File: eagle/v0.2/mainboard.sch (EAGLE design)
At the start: 40 parts, among them IC1 74HCT151D, IC2 74HCT151D, IC3 74HCT151D, IC4 74HCT151D, IC5 74HCT151D, IC6 74HCT151D, IC7 74HC590D, IC8 74HC02D, J1 629722000214, J2 629722000214, J3 629722000214, J4 629722000214, J5 629722000214, J7 L77HDE15SD1CH4RHNVGA

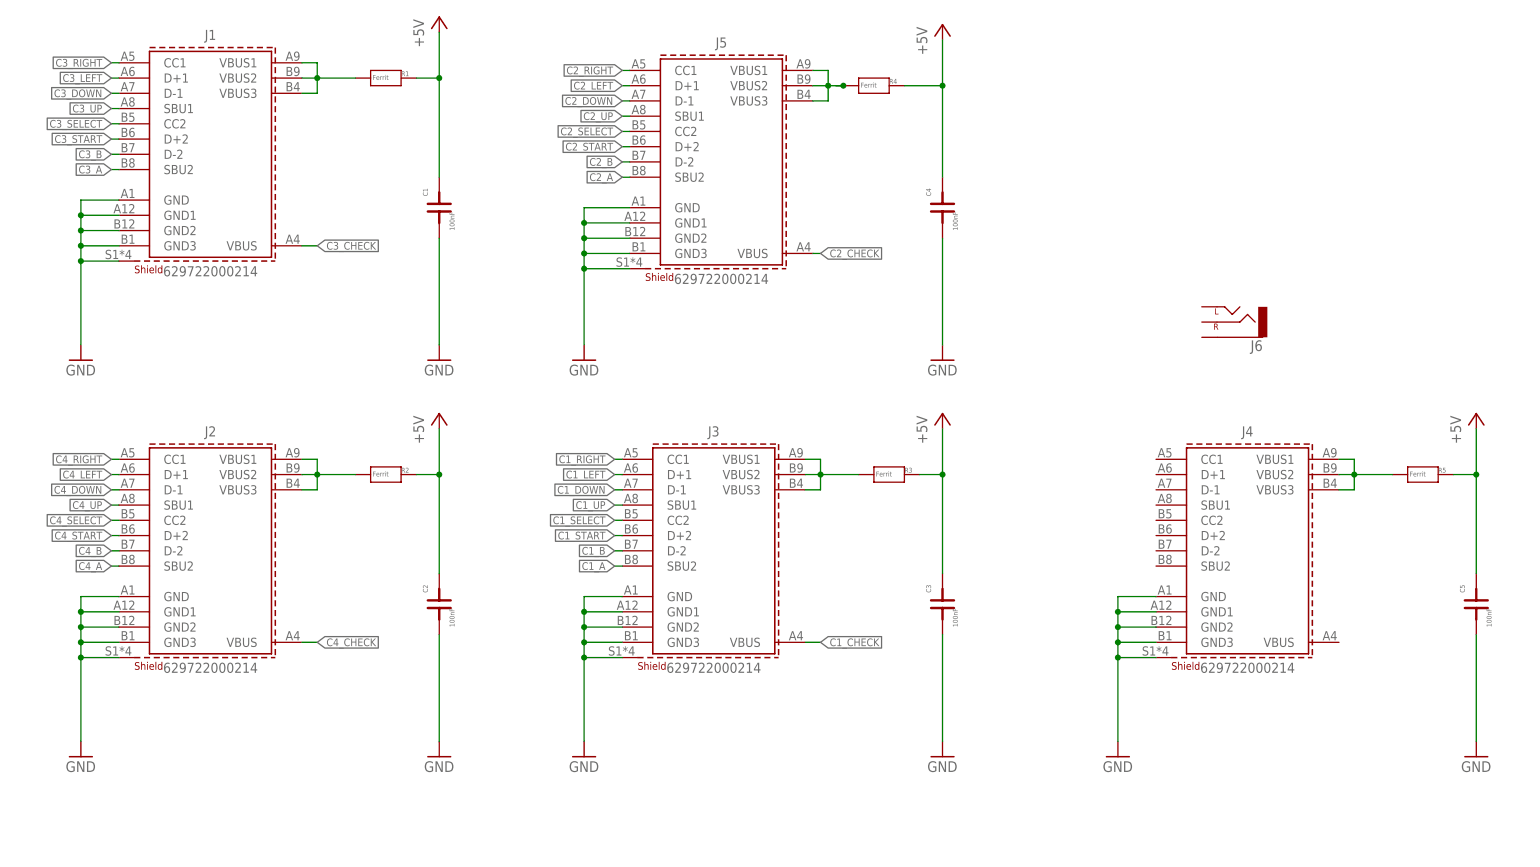
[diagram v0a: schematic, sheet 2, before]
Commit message: updated USB-C receptacles and würth library
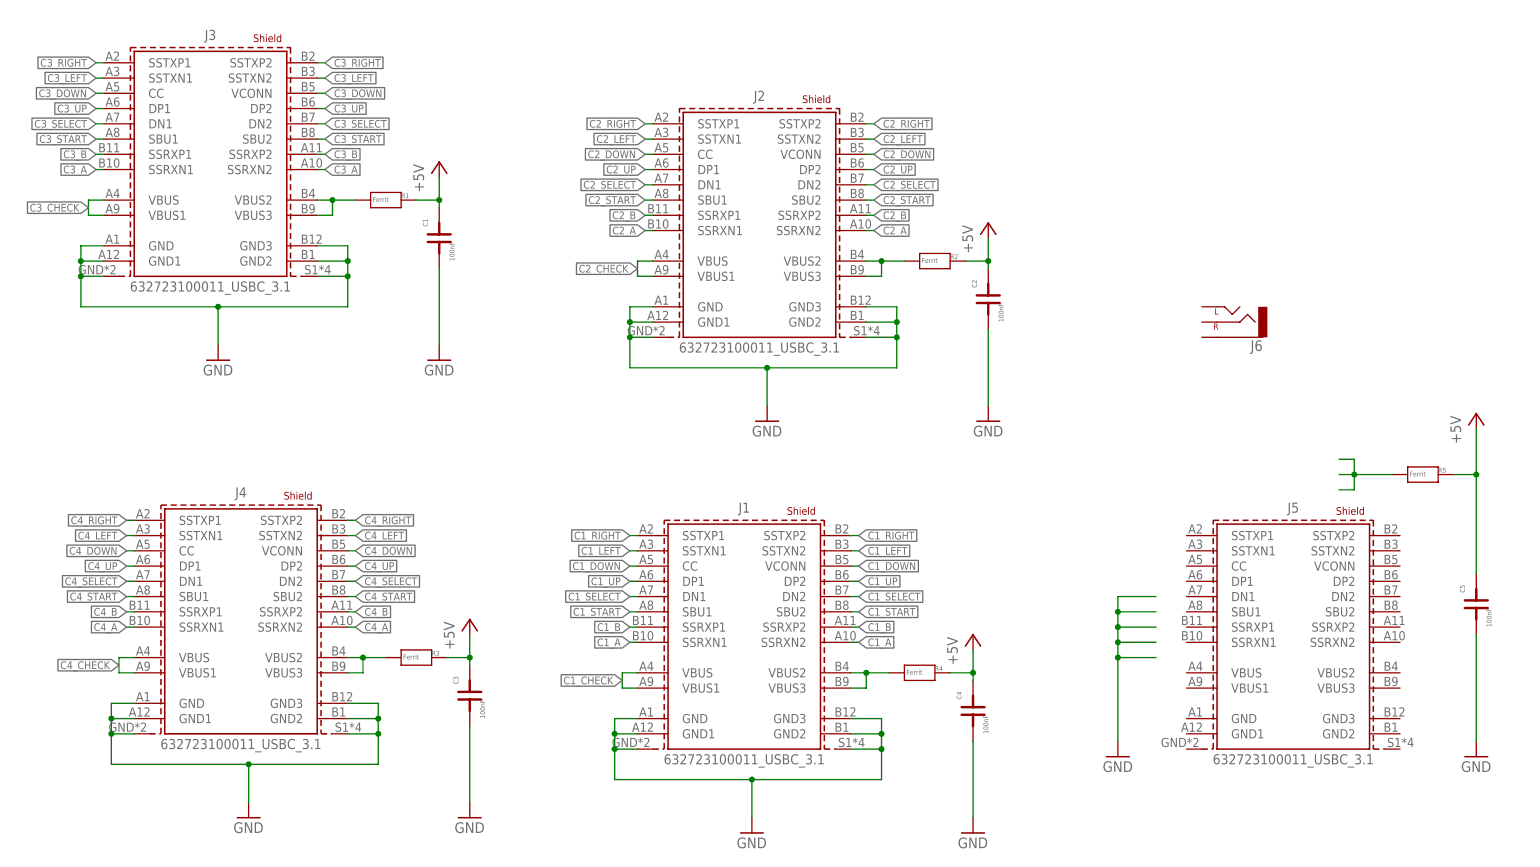
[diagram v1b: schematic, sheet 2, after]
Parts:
- J1, J2, J3, J4, J5: value 629722000214 -> 632723100011_USBC_3.1; device Eagle_WR-USB (rev22c):629722000214_CUSTOM -> Eagle_WR-USB (rev22c):632723100011_USBC_3.1
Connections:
- removed net N$26: J1.VBUS1, J1.VBUS2, J1.VBUS3, R1.1
- new net N$3: J3.VBUS2, J3.VBUS3, R1.1
- net C1_A: now also J1.SSRXN1, J1.SSRXN2; no longer J3.SBU2
- net C1_B: now also J1.SSRXP1, J1.SSRXP2; no longer J3.D-2
- net C1_CHECK: now also J1.VBUS, J1.VBUS1; no longer J3.VBUS
- net C1_DOWN: now also J1.CC, J1.VCONN; no longer J3.D-1
- net C1_LEFT: now also J1.SSTXN1, J1.SSTXN2; no longer J3.D+1
- net C1_RIGHT: now also J1.SSTXP1, J1.SSTXP2; no longer J3.CC1
- net C1_SELECT: now also J1.DN1, J1.DN2; no longer J3.CC2
- net C1_START: now also J1.SBU1, J1.SBU2; no longer J3.D+2
- net C1_UP: now also J1.DP1, J1.DP2; no longer J3.SBU1
- net C2_A: now also J2.SSRXN1, J2.SSRXN2; no longer J5.SBU2
- net C2_B: now also J2.SSRXP1, J2.SSRXP2; no longer J5.D-2
- net C2_CHECK: now also J2.VBUS, J2.VBUS1; no longer J5.VBUS
- net C2_DOWN: now also J2.CC, J2.VCONN; no longer J5.D-1
- net C2_LEFT: now also J2.SSTXN1, J2.SSTXN2; no longer J5.D+1
- net C2_RIGHT: now also J2.SSTXP1, J2.SSTXP2; no longer J5.CC1
- net C2_SELECT: now also J2.DN1, J2.DN2; no longer J5.CC2
- net C2_START: now also J2.SBU1, J2.SBU2; no longer J5.D+2
- net C2_UP: now also J2.DP1, J2.DP2; no longer J5.SBU1
- net C3_A: now also J3.SSRXN1, J3.SSRXN2; no longer J1.SBU2
- net C3_B: now also J3.SSRXP1, J3.SSRXP2; no longer J1.D-2
- net C3_CHECK: now also J3.VBUS, J3.VBUS1; no longer J1.VBUS
- net C3_DOWN: now also J3.CC, J3.VCONN; no longer J1.D-1
- net C3_LEFT: now also J3.SSTXN1, J3.SSTXN2; no longer J1.D+1
- net C3_RIGHT: now also J3.SSTXP1, J3.SSTXP2; no longer J1.CC1
- net C3_SELECT: now also J3.DN1, J3.DN2; no longer J1.CC2
- net C3_START: now also J3.SBU1, J3.SBU2; no longer J1.D+2
- net C3_UP: now also J3.DP1, J3.DP2; no longer J1.SBU1
- net C4_A: now also J4.SSRXN1, J4.SSRXN2; no longer J2.SBU2
- net C4_B: now also J4.SSRXP1, J4.SSRXP2; no longer J2.D-2
- net C4_CHECK: now also J4.VBUS, J4.VBUS1; no longer J2.VBUS
- net C4_DOWN: now also J4.CC, J4.VCONN; no longer J2.D-1
- net C4_LEFT: now also J4.SSTXN1, J4.SSTXN2; no longer J2.D+1
- net C4_RIGHT: now also J4.SSTXP1, J4.SSTXP2; no longer J2.CC1
- net C4_SELECT: now also J4.DN1, J4.DN2; no longer J2.CC2
- net C4_START: now also J4.SBU1, J4.SBU2; no longer J2.D+2
- net C4_UP: now also J4.DP1, J4.DP2; no longer J2.SBU1
- net GND: now also J1.SHIELD1, J2.SHIELD1, J3.SHIELD1, J4.SHIELD1; no longer J5.GND, J5.GND1, J5.GND2, J5.GND3, J5.SHIELD
- net N$1: no longer J4.VBUS1, J4.VBUS2, J4.VBUS3
- net N$2: no longer J2.VBUS1
- net N$4: now also J4.VBUS2, J4.VBUS3, R3.1; no longer J5.VBUS1, J5.VBUS2, J5.VBUS3, R4.1
- net N$5: now also J1.VBUS2, J1.VBUS3, R4.1; no longer J3.VBUS1, J3.VBUS2, J3.VBUS3, R3.1
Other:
- moved on the sheet: C1, C2, C3, C4, R1, R2, R3, R4

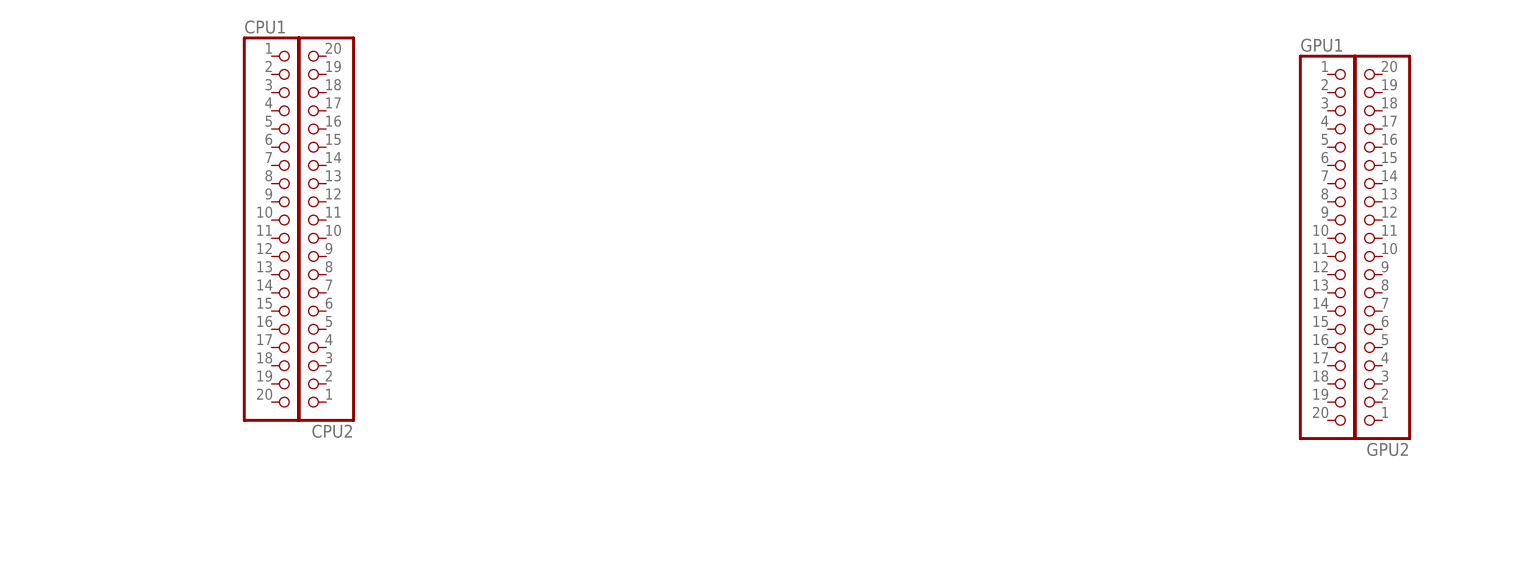
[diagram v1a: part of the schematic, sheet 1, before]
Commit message: renamed the pins for CPU and GPU
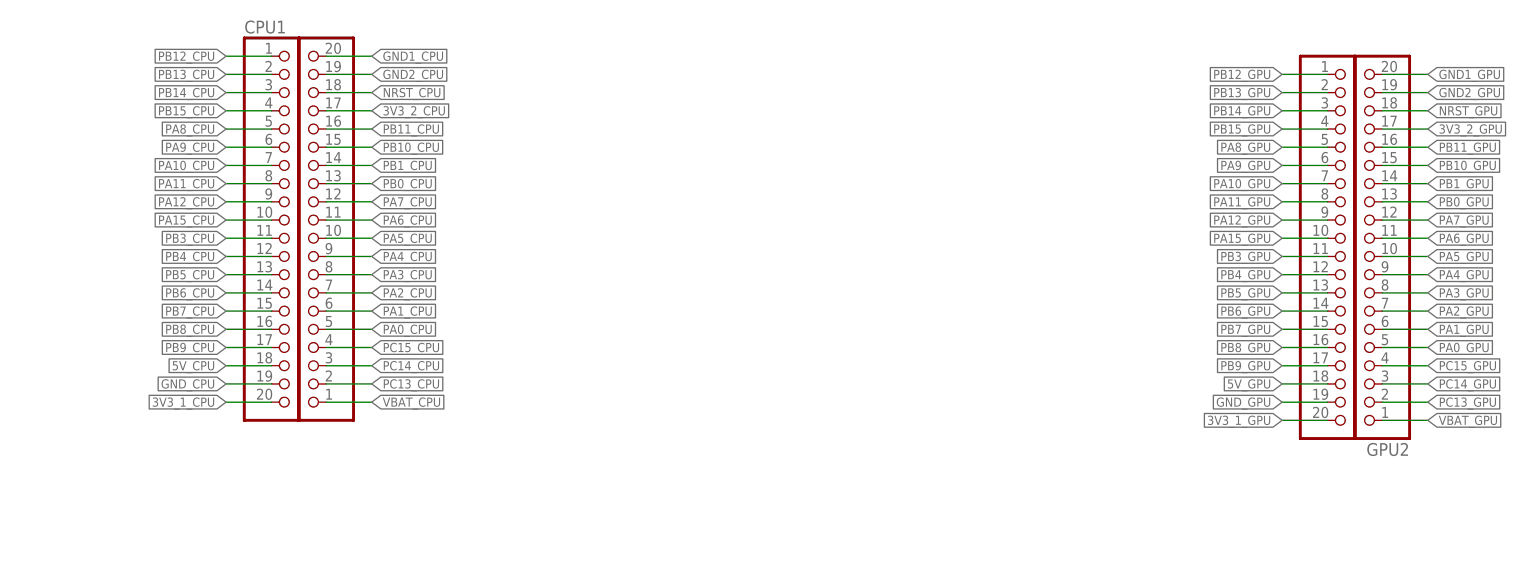
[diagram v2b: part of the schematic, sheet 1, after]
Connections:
- removed net DATA: IC6A.Y
- removed net SYNC: IC5A.Y
- new net 3V3_1_CPU: CPU1.20
- new net 3V3_1_GPU: GPU1.20
- new net 3V3_2_CPU: CPU2.17
- new net 3V3_2_GPU: GPU2.17
- new net 5V_CPU: CPU1.18
- new net 5V_GPU: GPU1.18
- new net GND1_CPU: CPU2.20
- new net GND1_GPU: GPU2.20
- new net GND2_CPU: CPU2.19
- new net GND2_GPU: GPU2.19
- new net GND_CPU: CPU1.19
- new net GND_GPU: GPU1.19
- new net NRST_CPU: CPU2.18
- new net NRST_GPU: GPU2.18
- new net PA0_CPU: CPU2.5
- new net PA0_GPU: GPU2.5
- new net PA10_CPU: CPU1.7
- new net PA10_GPU: GPU1.7
- new net PA11_CPU: CPU1.8
- new net PA11_GPU: GPU1.8
- new net PA12_CPU: CPU1.9
- new net PA12_GPU: GPU1.9
- new net PA15_CPU: CPU1.10
- new net PA15_GPU: GPU1.10
- new net PA1_CPU: CPU2.6
- new net PA1_GPU: GPU2.6
- new net PA2_CPU: CPU2.7
- new net PA2_GPU: GPU2.7
- new net PA3_CPU: CPU2.8
- new net PA3_GPU: GPU2.8
- new net PA4_CPU: CPU2.9
- new net PA4_GPU: GPU2.9
- new net PA5_CPU: CPU2.10
- new net PA5_GPU: GPU2.10
- new net PA6_CPU: CPU2.11
- new net PA6_GPU: GPU2.11
- new net PA7_CPU: CPU2.12
- new net PA7_GPU: GPU2.12
- new net PA8_CPU: CPU1.5
- new net PA8_GPU: GPU1.5
- new net PA9_CPU: CPU1.6
- new net PA9_GPU: GPU1.6
- new net PB0_CPU: CPU2.13
- new net PB0_GPU: GPU2.13
- new net PB10_CPU: CPU2.15
- new net PB10_GPU: GPU2.15
- new net PB11_CPU: CPU2.16
- new net PB11_GPU: GPU2.16
- new net PB12_CPU: CPU1.1
- new net PB12_GPU: GPU1.1
- new net PB13_CPU: CPU1.2
- new net PB13_GPU: GPU1.2
- new net PB14_CPU: CPU1.3
- new net PB14_GPU: GPU1.3
- new net PB15_CPU: CPU1.4
- new net PB15_GPU: GPU1.4
- new net PB1_CPU: CPU2.14
- new net PB1_GPU: GPU2.14
- new net PB3_CPU: CPU1.11
- new net PB3_GPU: GPU1.11
- new net PB4_CPU: CPU1.12
- new net PB4_GPU: GPU1.12
- new net PB5_CPU: CPU1.13
- new net PB5_GPU: GPU1.13
- new net PB6_CPU: CPU1.14
- new net PB6_GPU: GPU1.14
- new net PB7_CPU: CPU1.15
- new net PB7_GPU: GPU1.15
- new net PB8_CPU: CPU1.16
- new net PB8_GPU: GPU1.16
- new net PB9_CPU: CPU1.17
- new net PB9_GPU: GPU1.17
- new net PC13_CPU: CPU2.2
- new net PC13_GPU: GPU2.2
- new net PC14_CPU: CPU2.3
- new net PC14_GPU: GPU2.3
- new net PC15_CPU: CPU2.4
- new net PC15_GPU: GPU2.4
- new net VBAT_CPU: CPU2.1
- new net VBAT_GPU: GPU2.1

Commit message: cleaned up schemtic
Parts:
- removed R_BLUE1: 240R, rcl:R-EU_R0805
- removed R_BLUE2: 470R, rcl:R-EU_R0805
- removed R_BLUE3, R_GREEN4, R_RED4: 150, rcl:R-EU_R0805
- removed R_GREEN1, R_RED1: 270R, rcl:R-EU_R0805
- removed R_GREEN2, R_RED2: 560R, rcl:R-EU_R0805
- removed R_GREEN3, R_RED3: 1.1k, rcl:R-EU_R0805
- added C6, C7: 100nF, deto:C1
- added JP1: (no value), pinhead:PINHD-2X3
- added JP2, JP3, JP4: (no value), pinhead:PINHD-1X1
- added JP5: (no value), pinhead:PINHD-1X5
- added R10, R15, R20: 150, rcl:R-EU_R0805
- added R11, R16, R21, R22, R6: 1k, rcl:R-EU_R0805
- added R12, R17, R7: 100, rcl:R-EU_R0805
- added R13, R18, R8: 560, rcl:R-EU_R0805
- added R14, R19, R9: 270, rcl:R-EU_R0805
- added R23: 0, rcl:R-EU_R0805
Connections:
- removed net BLU1: R_BLUE1.1
- removed net BLU2: R_BLUE2.1
- removed net GRN1: R_GREEN1.1
- removed net GRN2: R_GREEN2.1
- removed net GRN3: R_GREEN3.1
- removed net N$6: J7.3, R_BLUE1.2, R_BLUE2.2, R_BLUE3.2
- removed net N$61: IC7A.CLK, IC7A.RCK
- removed net N$7: J7.1, R_RED1.2, R_RED2.2, R_RED3.2, R_RED4.2
- removed net RED1: R_RED1.1
- removed net RED2: R_RED2.1
- removed net RED3: R_RED3.1
- new net BLUE_LSP: R16.1
- new net BLUE_MMSP: R18.1
- new net BLUE_MSP: R19.1
- new net CLOCK: IC7A.CLK, IC7A.RCK, JP4.1, R23.1
- new net DATA: JP1.4, R21.1
- new net GREEN_LSP: R11.1
- new net GREEN_MMSP: R13.1
- new net GREEN_MSP: R14.1
- new net N$16: R6.2, R7.1
- new net N$18: R11.2, R12.1
- new net N$21: R16.2, R17.1
- new net N$23: JP1.5, JP3.1
- new net RED_LSP: R6.1
- new net RED_MMSP: R8.1
- new net RED_MSP: R9.1
- new net SYNC: JP1.3, R22.1
- new net VGA_BLUE: J7.2, R17.2, R18.2, R19.2, R20.2
- new net VGA_GREEN: J7.3, R12.2, R13.2, R14.2, R15.2
- new net VGA_RED: J7.1, R10.2, R7.2, R8.2, R9.2
- net C1_A: now also J4.SSRXP2; no longer J1.SSRXN1, J1.SSRXN2
- net C1_B: now also J4.SSRXN2; no longer J1.SSRXP1, J1.SSRXP2
- net C1_CHECK: now also J4.VBUS1; no longer J1.VBUS, J1.VBUS1
- net C1_DOWN: now also J4.CC; no longer J1.CC, J1.VCONN
- net C1_LEFT: now also J4.SSTXN1; no longer J1.SSTXN1, J1.SSTXN2
- net C1_RIGHT: now also J4.SSTXP1; no longer J1.SSTXP1, J1.SSTXP2
- net C1_SELECT: now also J4.DN1; no longer J1.DN1, J1.DN2
- net C1_START: now also J4.SBU1; no longer J1.SBU1, J1.SBU2
- net C1_UP: now also J4.DP1; no longer J1.DP1, J1.DP2
- net C2_A: now also J3.SSRXP2; no longer J2.SSRXN1, J2.SSRXN2
- net C2_B: now also J3.SSRXN2; no longer J2.SSRXP1, J2.SSRXP2
- net C2_CHECK: now also J3.VBUS1; no longer J2.VBUS, J2.VBUS1
- net C2_DOWN: now also J3.CC; no longer J2.CC, J2.VCONN
- net C2_LEFT: now also J3.SSTXN1; no longer J2.SSTXN1, J2.SSTXN2
- net C2_RIGHT: now also J3.SSTXP1; no longer J2.SSTXP1, J2.SSTXP2
- net C2_SELECT: now also J3.DN1; no longer J2.DN1, J2.DN2
- net C2_START: now also J3.SBU1; no longer J2.SBU1, J2.SBU2
- net C2_UP: now also J3.DP1; no longer J2.DP1, J2.DP2
- net C3_A: now also J1.SSRXP2; no longer J3.SSRXN1, J3.SSRXN2
- net C3_B: now also J1.SSRXN2; no longer J3.SSRXP1, J3.SSRXP2
- net C3_CHECK: now also J1.VBUS1; no longer J3.VBUS, J3.VBUS1
- net C3_DOWN: now also J1.CC; no longer J3.CC, J3.VCONN
- net C3_LEFT: now also J1.SSTXN1; no longer J3.SSTXN1, J3.SSTXN2
- net C3_RIGHT: now also J1.SSTXP1; no longer J3.SSTXP1, J3.SSTXP2
- net C3_SELECT: now also J1.DN1; no longer J3.DN1, J3.DN2
- net C3_START: now also J1.SBU1; no longer J3.SBU1, J3.SBU2
- net C3_UP: now also J1.DP1; no longer J3.DP1, J3.DP2
- net C4_A: now also J2.SSRXP2; no longer J4.SSRXN1, J4.SSRXN2
- net C4_B: now also J2.SSRXN2; no longer J4.SSRXP1, J4.SSRXP2
- net C4_CHECK: now also J2.VBUS1; no longer J4.VBUS, J4.VBUS1
- net C4_DOWN: now also J2.CC; no longer J4.CC, J4.VCONN
- net C4_LEFT: now also J2.SSTXN1; no longer J4.SSTXN1, J4.SSTXN2
- net C4_RIGHT: now also J2.SSTXP1; no longer J4.SSTXP1, J4.SSTXP2
- net C4_SELECT: now also J2.DN1; no longer J4.DN1, J4.DN2
- net C4_START: now also J2.SBU1; no longer J4.SBU1, J4.SBU2
- net C4_UP: now also J2.DP1; no longer J4.DP1, J4.DP2
- net GND: now also C6.1, C7.1, J5.GND, J5.GND1, J5.SHIELD, J5.SHIELD1, R10.1, R15.1, R20.1; no longer J1.GND2, J1.GND3, J2.GND2, J2.GND3, J3.GND2, J3.GND3, J4.GND2, J4.GND3, R_BLUE3.1, R_GREEN4.1, R_RED4.1
- net N$1: now also J5.VBUS, J5.VBUS1
- net N$10: now also JP5.2
- net N$11: now also JP5.3
- net N$19: now also JP5.5
- net N$2: now also J3.VBUS; no longer J2.VBUS2, J2.VBUS3
- net N$20: now also JP1.1
- net N$22: now also JP1.2
- net N$24: now also JP5.4
- net N$3: now also J1.VBUS; no longer J3.VBUS2, J3.VBUS3
- net N$4: now also J2.VBUS; no longer J4.VBUS2, J4.VBUS3
- net N$5: now also J4.VBUS; no longer J1.VBUS2, J1.VBUS3
- net N$8: now also JP1.6, JP2.1; no longer J7.2, R_GREEN1.2, R_GREEN2.2, R_GREEN3.2, R_GREEN4.2
- net N$9: now also JP5.1
- net PA10_CPU: now also C6.2, R22.2
- net PA8_CPU: now also R23.2
- net PA9_CPU: now also C7.2, R21.2

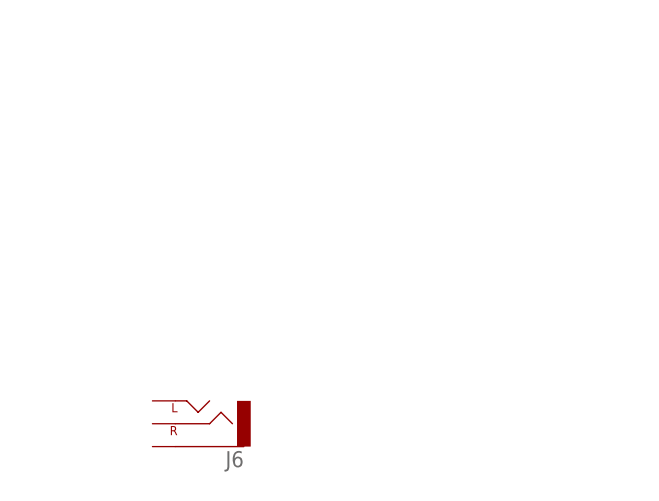
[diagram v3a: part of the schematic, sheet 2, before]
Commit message: added Board to board connector
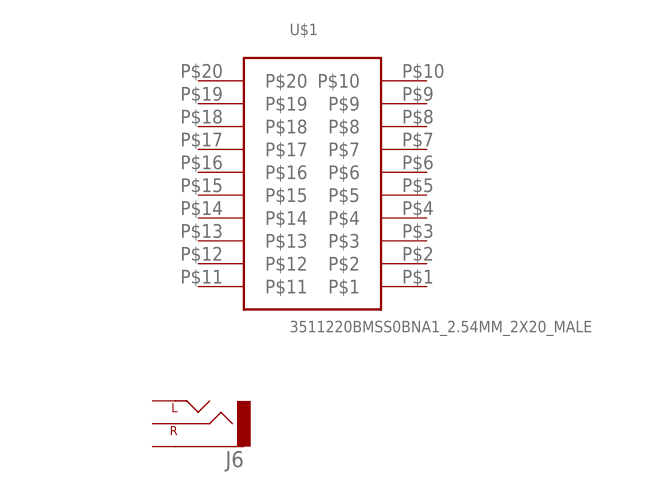
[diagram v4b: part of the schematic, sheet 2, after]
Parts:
- added U$1: 3511220BMSS0BNA1_2.54MM_2X20_MALE, BtoB_connector:3511220BMSS0BNA1_2.54MM_2X20_MALE
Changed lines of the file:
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@@
 <part name="GND14" library="supply1" library_urn="urn:adsk.eagle:library:371" deviceset="GND" device=""/>
 <part name="GND15" library="supply1" library_urn="urn:adsk.eagle:library:371" deviceset="GND" device=""/>
+<part name="U$1" library="BtoB_connector" deviceset="3511220BMSS0BNA1_2.54MM_2X20_MALE" device=""/>
 </parts>
 <sheets>
@@
 <attribute name="VALUE" x="210.82" y="63.5" size="1.6764" layer="96" align="bottom-center"/>
 </instance>
+<instance part="U$1" gate="G$1" x="218.44" y="147.32" smashed="yes">
+<attribute name="NAME" x="215.9" y="165.1" size="1.27" layer="95"/>
+<attribute name="VALUE" x="215.9" y="132.08" size="1.27" layer="96"/>
+</instance>
 </instances>
